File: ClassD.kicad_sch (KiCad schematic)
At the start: 8 parts, among them J1 Conn_01x02_Pin, U1 L78L09_TO92

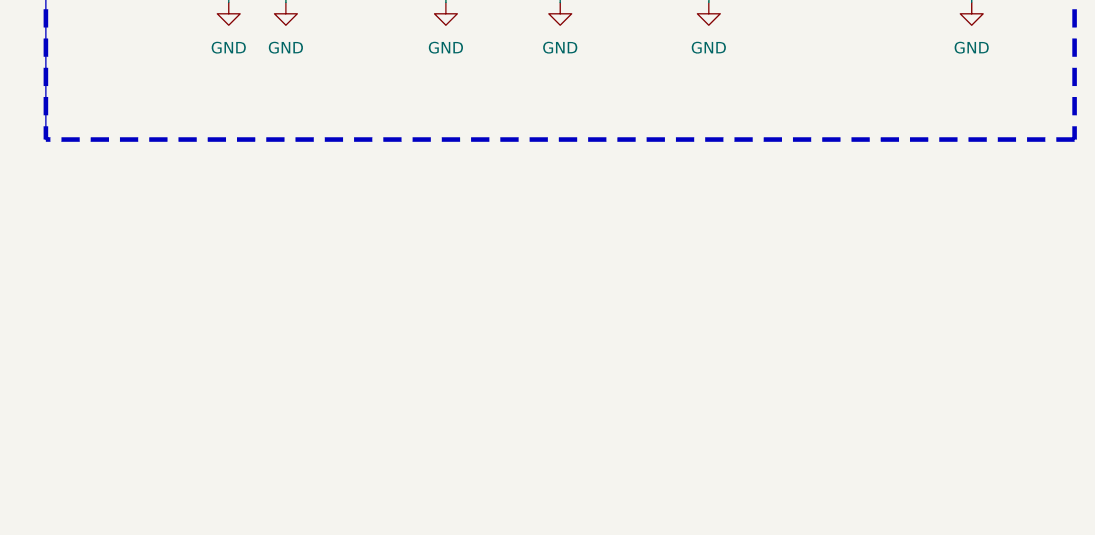
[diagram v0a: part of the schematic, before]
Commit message: Added audio input
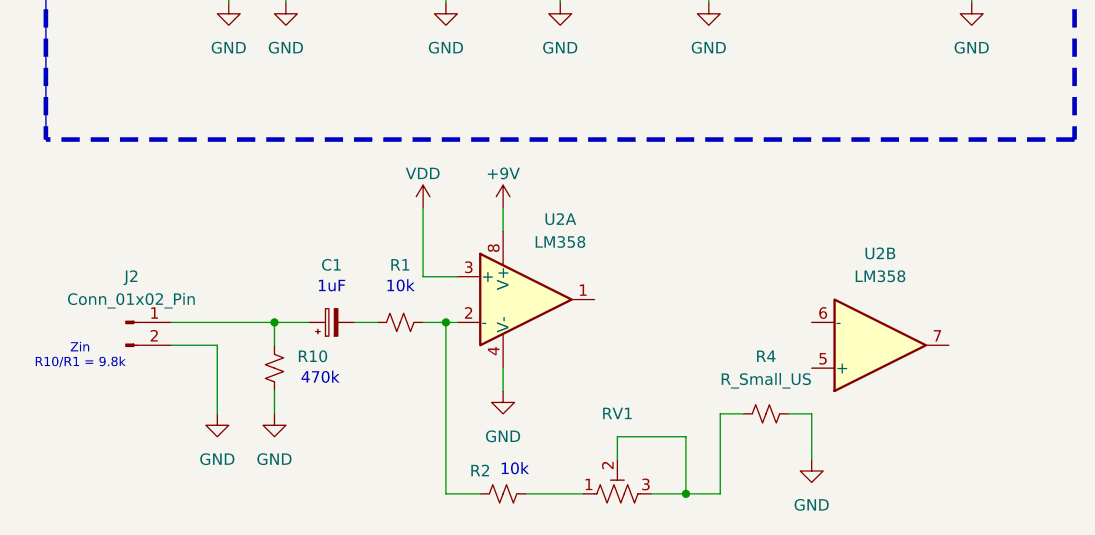
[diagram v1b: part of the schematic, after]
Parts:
- added C1: C_Polarized_Small, symbol Device:C_Polarized_Small
- added J2: Conn_01x02_Pin, symbol Connector:Conn_01x02_Pin
- added R1, R10, R2, R4: R_Small_US, symbol Device:R_Small_US
- added RV1: R_Potentiometer_Trim_US, symbol Device:R_Potentiometer_Trim_US
- added U2: LM358, symbol Amplifier_Operational:LM358
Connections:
- net +9V: now also U2.8 (V+)
- net GND: now also J2.2 (Pin_2), R10.2, R4.2, U2.4 (V-)
- new net: R2.2, RV1.1
- new net: R4.1, RV1.2, RV1.3
- new net: R1.2, R2.1, U2.2 (-)
- new net: C1.1, J2.1 (Pin_1), R10.1
- new net: C1.2, R1.1
- new net VDD: U2.3 (+)
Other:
- note added: "470k"
- note added: "Zin R10/R1 = 9.8k"

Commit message: Finished Schematic Class D
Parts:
- added C4, C5, C8: C_Small, symbol Device:C_Small
- added C6, C9: C_Small_US, symbol Device:C_Small_US
- added H1, H2, H3, H4: MountingHole, symbol Mechanical:MountingHole
- added J3: Conn_01x03, symbol Connector_Generic:Conn_01x03
- added R12, R4, R6, R7, R8: R_Small_US, symbol Device:R_Small_US
- added RV3: R_Potentiometer_Trim_US, symbol Device:R_Potentiometer_Trim_US
- added TP1, TP2, TP3, TP4, TP5, TP6, TP7, TP8: TestPoint, symbol Connector:TestPoint_Small
- added U3: TL494, symbol Regulator_Controller:TL494
- renumbered R4 to R11
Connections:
- net +12V: now also C9.1, R8.1, TP4.1, U3.11 (C2), U3.12 (VCC)
- net +9V: now also C4.1, TP3.1
- net GND: now also C4.2, C8.2, C9.2, J3.2 (Pin_2), R12.2, R7.2, TP2.1, U3.13 (OUTCTRL), U3.16 (2IN+), U3.4 (DTC), U3.7 (GND), U3.9 (E1)
- net VDC: now also U2.5 (+), TP1.1
- net at R11.1, RV1.2, RV1.3: now also U2.1, R4.1
- net at U2.6 (-): now also C5.1, C6.2, R6.1
- net AUDIO: now reaches U2.7
- net AUDIO: now also C5.2, R12.1, R6.2, TP7.1, U3.1 (1IN+)
- new net: R7.1, RV3.3
- new net: C6.1, R4.2
- new net: U3.14 (REF), U3.15 (2IN-)
- new net: RV3.1, RV3.2, U3.6 (RT)
- new net !PWM: J3.3 (Pin_3), TP5.1, U3.10 (E2)
- new net FB: U3.2 (1IN-), U3.3 (FB)
- new net PWM: J3.1 (Pin_1), R8.2, TP6.1, U3.8 (C1)
- new net SAWTOOTH: C8.1, TP8.1, U3.5 (CT)
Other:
- note added: "* All capacitors (C) should be rated at least 25V"
- note added: "* All resistors (R) should handle at least 1/4 W"
- note added: "* RV2 Should be adjusted to 50% duty cycle in either PWM or !PWM when no audio is connected"
- note added: "100k"
- note added: "100nF"
- note added: "100uF"
- note added: "10uF"
- note added: "1k"
- note added: "1nF"
- note added: "3.3k"
- note added: "8.2k"
- note added: "82k"
- note added: "@Mundo Electronica"
- note added: "Gain (1-11)X"
- note added: "Power Stage"
- note added: "Preamplification / Audio Filtering / Test Points"
- note added: "Pulse Width Modulation (PWM) / Mounting Holes"
- note removed: "POWER STAGE"
- title: (none) -> ENGG220 Final Project - Victor Rosales
- moved on the sheet: C1, C10, C2, C3, J1, J2, R1, R10, R11, R2, R3, R5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
